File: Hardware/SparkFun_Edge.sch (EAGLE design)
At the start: 64 parts, among them J5 CORTEX_DEBUG, J7 CAMERA-HIMAX, U2 LIS2DH12, U3 1.8V, U5 ARTEMIS_MODULESMD, Y2 32.768kHz

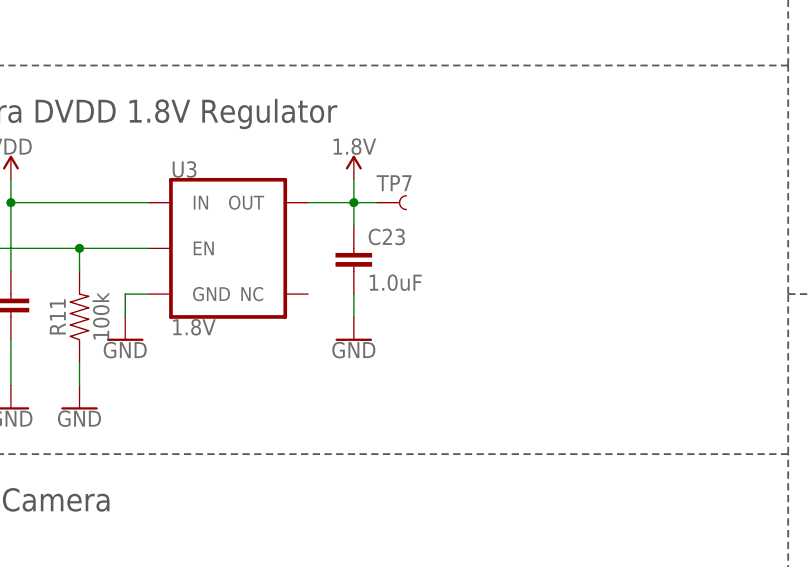
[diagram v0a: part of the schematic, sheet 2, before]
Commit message: Rename files. Remove dependancy on Ambiq lbr. Remove ambiq.lbr.
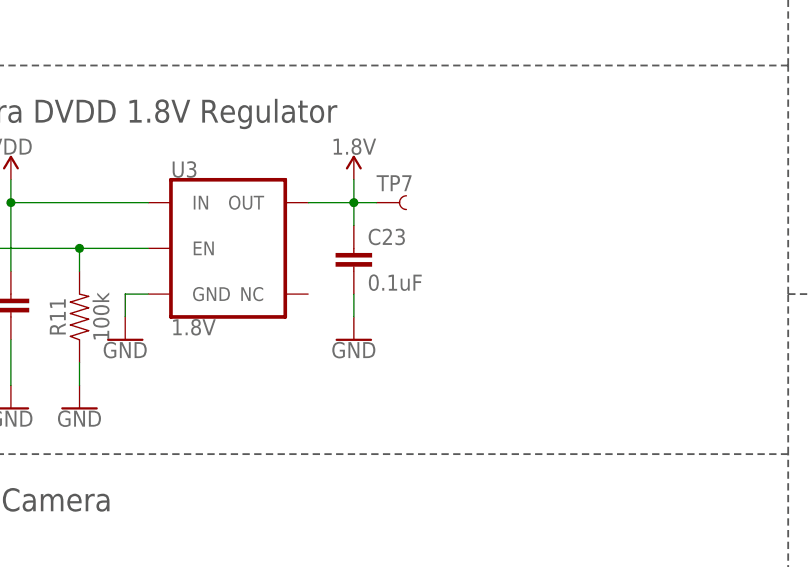
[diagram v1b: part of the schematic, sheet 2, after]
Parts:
- C1, C18, C20: device ambiq:0.1UF-0402-TIGHT-16V-10% -> SparkFun-Capacitors:0.1UF-0402T-16V-10%
- C10, C9: device ambiq:15PF-0402-TIGHT-50V-5% -> SparkFun-Capacitors:15PF-0402T-50V-5%
- C22: device ambiq:1.0UF-0402-TIGHT-16V-10% -> SparkFun-Capacitors:1.0UF-0402T-16V-10%
- C23: value 1.0uF -> 0.1uF; device ambiq:1.0UF-0402-TIGHT-16V-10% -> SparkFun-Capacitors:0.1UF-0402T-16V-10%
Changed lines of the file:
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@@
 <?xml version="1.0" encoding="utf-8"?>
 <!DOCTYPE eagle SYSTEM "eagle.dtd">
-<eagle version="9.5.1">
+<eagle version="9.4.2">
 <drawing>
 <settings>
@@
 <part name="J2" library="SparkFun-Connectors" deviceset="6_PIN_SERIAL_TARGET" device="SMD"/>
 <part name="Y2" library="SparkFun-Clocks" deviceset="CRYSTAL-32.768KHZ" device="SMD-3.2X1.5" value="32.768kHz"/>
-<part name="C9" library="ambiq" deviceset="15PF" device="-0402-TIGHT-50V-5%" value="15pF"/>
-<part name="C10" library="ambiq" deviceset="15PF" device="-0402-TIGHT-50V-5%" value="15pF"/>
+<part name="C9" library="SparkFun-Capacitors" deviceset="15PF" device="-0402T-50V-5%" value="15pF"/>
+<part name="C10" library="SparkFun-Capacitors" deviceset="15PF" device="-0402T-50V-5%" value="15pF"/>
 <part name="GND19" library="SparkFun-PowerSymbols" deviceset="GND" device=""/>
 <part name="GND24" library="SparkFun-PowerSymbols" deviceset="GND" device=""/>
@@
 <part name="U2" library="SparkFun-Sensors" deviceset="LIS2DH12" device=""/>
 <part name="C21" library="SparkFun-Capacitors" deviceset="10UF" device="-0603-6.3V-20%" value="10uF"/>
-<part name="C20" library="ambiq" deviceset="0.1UF" device="-0402-TIGHT-16V-10%" value="0.1uF"/>
+<part name="C20" library="SparkFun-Capacitors" deviceset="0.1UF" device="-0402T-16V-10%" value="0.1uF"/>
 <part name="GND31" library="SparkFun-PowerSymbols" deviceset="GND" device=""/>
 <part name="GND29" library="SparkFun-PowerSymbols" deviceset="GND" device=""/>
@@
 <part name="GND34" library="SparkFun-PowerSymbols" deviceset="GND" device=""/>
 <part name="SUPPLY28" library="SparkFun-PowerSymbols" deviceset="1.8V" device=""/>
-<part name="C22" library="ambiq" deviceset="1.0UF" device="-0402-TIGHT-16V-10%" value="1.0uF"/>
-<part name="C23" library="ambiq" deviceset="1.0UF" device="-0402-TIGHT-16V-10%" value="1.0uF"/>
+<part name="C22" library="SparkFun-Capacitors" deviceset="1.0UF" device="-0402T-16V-10%" value="1.0uF"/>
+<part name="C23" library="SparkFun-Capacitors" deviceset="0.1UF" device="-0402T-16V-10%" value="0.1uF"/>
 <part name="GND35" library="SparkFun-PowerSymbols" deviceset="GND" device=""/>
 <part name="GND30" library="SparkFun-PowerSymbols" deviceset="GND" device=""/>
@@
 <part name="GND45" library="SparkFun-PowerSymbols" deviceset="GND" device=""/>
 <part name="GND17" library="SparkFun-PowerSymbols" deviceset="GND" device=""/>
-<part name="C18" library="ambiq" deviceset="0.1UF" device="-0402-TIGHT-16V-10%" value="0.1uF"/>
+<part name="C18" library="SparkFun-Capacitors" deviceset="0.1UF" device="-0402T-16V-10%" value="0.1uF"/>
 <part name="GND21" library="SparkFun-PowerSymbols" deviceset="GND" device=""/>
 <part name="GND36" library="SparkFun-PowerSymbols" deviceset="GND" device=""/>
@@
 <part name="GND7" library="SparkFun-PowerSymbols" deviceset="GND" device=""/>
 <part name="E2" library="SparkFun-Sensors" deviceset="SPH0641LM4H-1_MICROPHONE" device="" value="SPH0641LM4H-1"/>
-<part name="C1" library="ambiq" deviceset="0.1UF" device="-0402-TIGHT-16V-10%" value="0.1uF"/>
+<part name="C1" library="SparkFun-Capacitors" deviceset="0.1UF" device="-0402T-16V-10%" value="0.1uF"/>
 <part name="GND2" library="SparkFun-PowerSymbols" deviceset="GND" device=""/>
 <part name="GND8" library="SparkFun-PowerSymbols" deviceset="GND" device=""/>

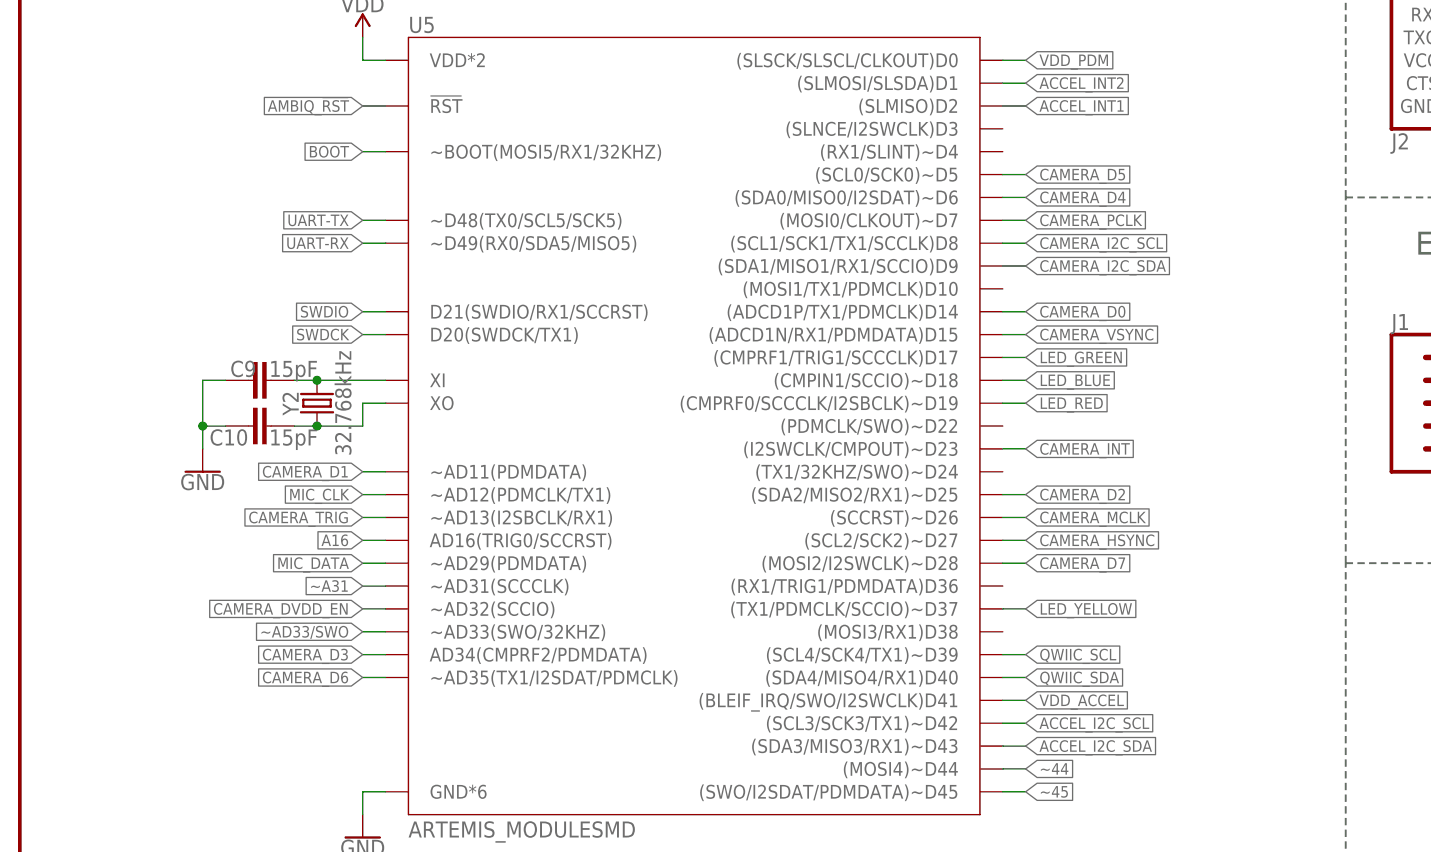
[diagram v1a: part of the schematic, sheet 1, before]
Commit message: add gpio numbers to camera nets for ease of use
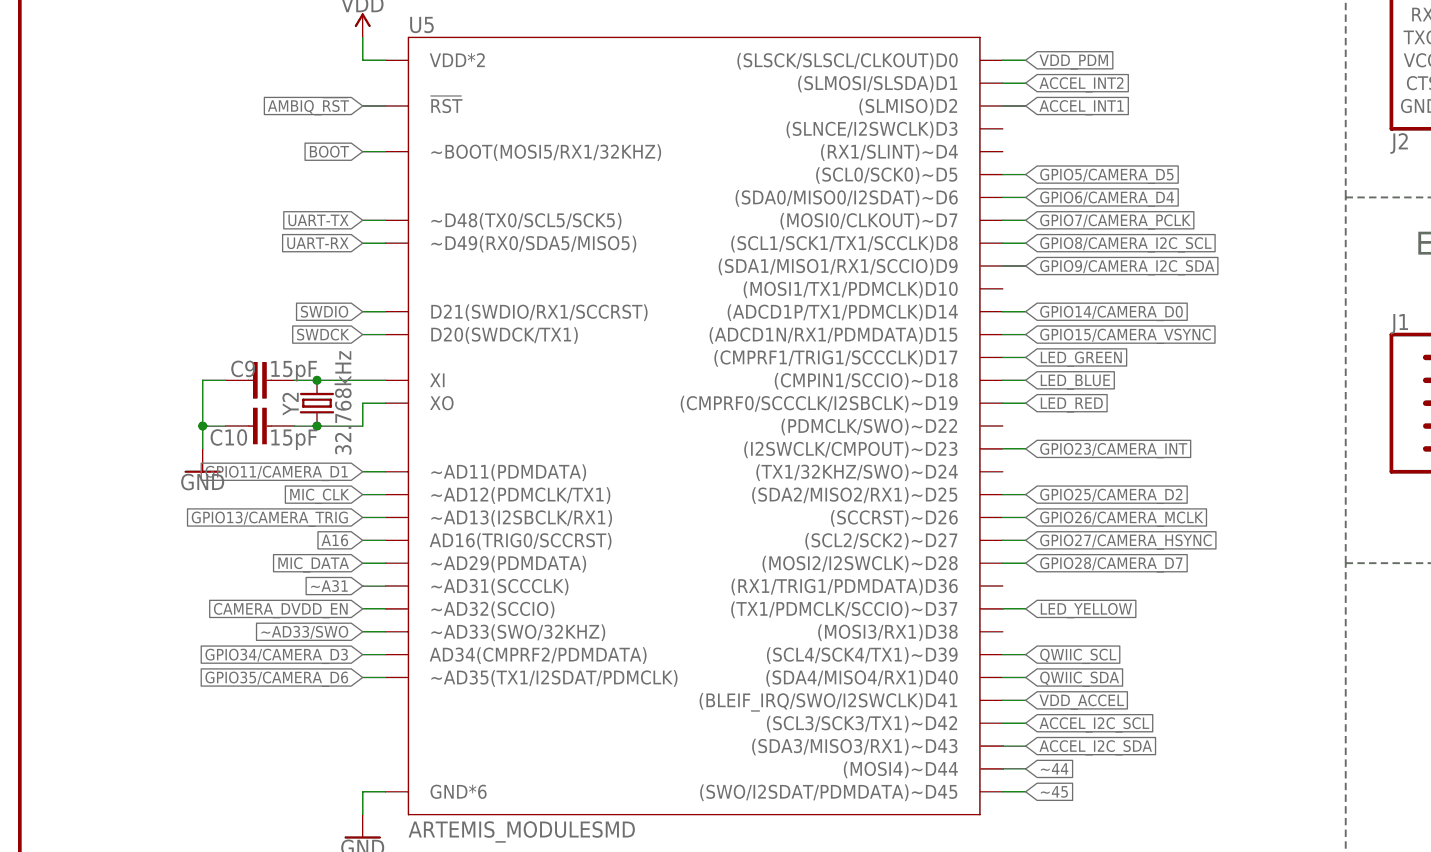
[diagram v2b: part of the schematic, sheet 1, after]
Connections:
- net CAMERA_D0 renamed GPIO14/CAMERA_D0
- net CAMERA_D1 renamed GPIO11/CAMERA_D1
- net CAMERA_D2 renamed GPIO25/CAMERA_D2
- net CAMERA_D3 renamed GPIO34/CAMERA_D3
- net CAMERA_D4 renamed GPIO6/CAMERA_D4
- net CAMERA_D5 renamed GPIO5/CAMERA_D5
- net CAMERA_D6 renamed GPIO35/CAMERA_D6
- net CAMERA_D7 renamed GPIO28/CAMERA_D7
- net CAMERA_HSYNC renamed GPIO27/CAMERA_HSYNC
- net CAMERA_I2C_SCL renamed GPIO8/CAMERA_I2C_SCL
- net CAMERA_I2C_SDA renamed GPIO9/CAMERA_I2C_SDA
- net CAMERA_INT renamed GPIO23/CAMERA_INT
- net CAMERA_MCLK renamed GPIO26/CAMERA_MCLK
- net CAMERA_PCLK renamed GPIO7/CAMERA_PCLK
- net CAMERA_TRIG renamed GPIO13/CAMERA_TRIG
- net CAMERA_VSYNC renamed GPIO15/CAMERA_VSYNC
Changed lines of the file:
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@@
 <?xml version="1.0" encoding="utf-8"?>
 <!DOCTYPE eagle SYSTEM "eagle.dtd">
-<eagle version="9.4.2">
+<eagle version="9.5.0">
 <drawing>
 <settings>
@@
 </segment>
 </net>
-<net name="CAMERA_VSYNC" class="0">
+<net name="GPIO15/CAMERA_VSYNC" class="0">
 <segment>
 <wire x1="109.22" y1="93.98" x2="111.76" y2="93.98" width="0.1524" layer="91"/>
@@
 </segment>
 </net>
-<net name="CAMERA_INT" class="0">
+<net name="GPIO23/CAMERA_INT" class="0">
 <segment>
 <wire x1="109.22" y1="81.28" x2="111.76" y2="81.28" width="0.1524" layer="91"/>
@@
 </segment>
 </net>
-<net name="CAMERA_I2C_SDA" class="0">
-<segment>
-<wire x1="109.22" y1="101.6" x2="111.76" y2="101.6" width="0.1524" layer="91"/>
-<label x="111.76" y="101.6" size="1.27" layer="95" xref="yes"/>
-<pinref part="U5" gate="U1" pin="(SDA1/MISO1/RX1/SCCIO)D9"/>
-</segment>
-</net>
-<net name="CAMERA_I2C_SCL" class="0">
+<net name="GPIO8/CAMERA_I2C_SCL" class="0">
 <segment>
 <wire x1="109.22" y1="104.14" x2="111.76" y2="104.14" width="0.1524" layer="91"/>
@@
 </segment>
 </net>
-<net name="CAMERA_TRIG" class="0">
+<net name="GPIO13/CAMERA_TRIG" class="0">
 <segment>
 <wire x1="40.64" y1="73.66" x2="38.1" y2="73.66" width="0.1524" layer="91"/>
@@
 </segment>
 </net>
-<net name="CAMERA_HSYNC" class="0">
+<net name="GPIO27/CAMERA_HSYNC" class="0">
 <segment>
 <wire x1="109.22" y1="71.12" x2="111.76" y2="71.12" width="0.1524" layer="91"/>
@@
 </segment>
 </net>
-<net name="CAMERA_D7" class="0">
+<net name="GPIO28/CAMERA_D7" class="0">
 <segment>
 <wire x1="109.22" y1="68.58" x2="111.76" y2="68.58" width="0.1524" layer="91"/>
@@
 </segment>
 </net>
-<net name="CAMERA_D6" class="0">
+<net name="GPIO35/CAMERA_D6" class="0">
 <segment>
 <wire x1="40.64" y1="55.88" x2="38.1" y2="55.88" width="0.1524" layer="91"/>
@@
 </segment>
 </net>
-<net name="CAMERA_D5" class="0">
+<net name="GPIO5/CAMERA_D5" class="0">
 <segment>
 <wire x1="109.22" y1="111.76" x2="111.76" y2="111.76" width="0.1524" layer="91"/>
@@
 </segment>
 </net>
-<net name="CAMERA_PCLK" class="0">
+<net name="GPIO7/CAMERA_PCLK" class="0">
 <segment>
 <wire x1="109.22" y1="106.68" x2="111.76" y2="106.68" width="0.1524" layer="91"/>
@@
 </segment>
 </net>
-<net name="CAMERA_D4" class="0">
+<net name="GPIO6/CAMERA_D4" class="0">
 <segment>
 <wire x1="109.22" y1="109.22" x2="111.76" y2="109.22" width="0.1524" layer="91"/>
@@
 </segment>
 </net>
-<net name="CAMERA_D0" class="0">
+<net name="GPIO14/CAMERA_D0" class="0">
 <segment>
 <wire x1="109.22" y1="96.52" x2="111.76" y2="96.52" width="0.1524" layer="91"/>
@@
 </segment>
 </net>
-<net name="CAMERA_D3" class="0">
+<net name="GPIO34/CAMERA_D3" class="0">
 <segment>
 <wire x1="40.64" y1="58.42" x2="38.1" y2="58.42" width="0.1524" layer="91"/>
@@
 </segment>
 </net>
-<net name="CAMERA_D1" class="0">
+<net name="GPIO11/CAMERA_D1" class="0">
 <segment>
 <wire x1="40.64" y1="78.74" x2="38.1" y2="78.74" width="0.1524" layer="91"/>
@@
 </segment>
 </net>
-<net name="CAMERA_D2" class="0">
+<net name="GPIO25/CAMERA_D2" class="0">
 <segment>
 <wire x1="109.22" y1="76.2" x2="111.76" y2="76.2" width="0.1524" layer="91"/>
@@
 </segment>
 </net>
-<net name="CAMERA_MCLK" class="0">
+<net name="GPIO26/CAMERA_MCLK" class="0">
 <segment>
 <wire x1="109.22" y1="73.66" x2="111.76" y2="73.66" width="0.1524" layer="91"/>
@@
 <wire x1="109.22" y1="53.34" x2="111.76" y2="53.34" width="0.1524" layer="91"/>
 <label x="111.76" y="53.34" size="1.27" layer="95" xref="yes"/>
+</segment>
+</net>
+<net name="GPIO9/CAMERA_I2C_SDA" class="0">
+<segment>
+<wire x1="109.22" y1="101.6" x2="111.76" y2="101.6" width="0.1524" layer="91"/>
+<label x="111.76" y="101.6" size="1.27" layer="95" xref="yes"/>
+<pinref part="U5" gate="U1" pin="(SDA1/MISO1/RX1/SCCIO)D9"/>
 </segment>
 </net>
@@
 </segment>
 </net>
-<net name="CAMERA_I2C_SCL" class="0">
+<net name="GPIO8/CAMERA_I2C_SCL" class="0">
 <segment>
 <wire x1="86.36" y1="58.42" x2="88.9" y2="58.42" width="0.1524" layer="91"/>
@@
 </segment>
 </net>
-<net name="CAMERA_I2C_SDA" class="0">
+<net name="GPIO9/CAMERA_I2C_SDA" class="0">
 <segment>
 <wire x1="86.36" y1="55.88" x2="88.9" y2="55.88" width="0.1524" layer="91"/>
@@
 </segment>
 </net>
-<net name="CAMERA_D1" class="0">
+<net name="GPIO11/CAMERA_D1" class="0">
 <segment>
 <wire x1="86.36" y1="33.02" x2="88.9" y2="33.02" width="0.1524" layer="91"/>
@@
 </segment>
 </net>
-<net name="CAMERA_D3" class="0">
+<net name="GPIO34/CAMERA_D3" class="0">
 <segment>
 <wire x1="86.36" y1="27.94" x2="88.9" y2="27.94" width="0.1524" layer="91"/>
@@
 </segment>
 </net>
-<net name="CAMERA_D4" class="0">
+<net name="GPIO6/CAMERA_D4" class="0">
 <segment>
 <wire x1="86.36" y1="25.4" x2="88.9" y2="25.4" width="0.1524" layer="91"/>
@@
 </segment>
 </net>
-<net name="CAMERA_D5" class="0">
+<net name="GPIO5/CAMERA_D5" class="0">
 <segment>
 <wire x1="86.36" y1="22.86" x2="88.9" y2="22.86" width="0.1524" layer="91"/>
@@
 </segment>
 </net>
-<net name="CAMERA_D6" class="0">
+<net name="GPIO35/CAMERA_D6" class="0">
 <segment>
 <wire x1="86.36" y1="20.32" x2="88.9" y2="20.32" width="0.1524" layer="91"/>
@@
 </segment>
 </net>
-<net name="CAMERA_D7" class="0">
+<net name="GPIO28/CAMERA_D7" class="0">
 <segment>
 <wire x1="86.36" y1="17.78" x2="88.9" y2="17.78" width="0.1524" layer="91"/>
@@
 </segment>
 </net>
-<net name="CAMERA_VSYNC" class="0">
+<net name="GPIO15/CAMERA_VSYNC" class="0">
 <segment>
 <wire x1="86.36" y1="50.8" x2="88.9" y2="50.8" width="0.1524" layer="91"/>
@@
 </segment>
 </net>
-<net name="CAMERA_HSYNC" class="0">
+<net name="GPIO27/CAMERA_HSYNC" class="0">
 <segment>
 <wire x1="86.36" y1="48.26" x2="88.9" y2="48.26" width="0.1524" layer="91"/>
@@
 </segment>
 </net>
-<net name="CAMERA_PCLK" class="0">
+<net name="GPIO7/CAMERA_PCLK" class="0">
 <segment>
 <wire x1="86.36" y1="40.64" x2="88.9" y2="40.64" width="0.1524" layer="91"/>
@@
 </segment>
 </net>
-<net name="CAMERA_D0" class="0">
+<net name="GPIO14/CAMERA_D0" class="0">
 <segment>
 <wire x1="86.36" y1="35.56" x2="88.9" y2="35.56" width="0.1524" layer="91"/>
@@
 </segment>
 </net>
-<net name="CAMERA_D2" class="0">
+<net name="GPIO25/CAMERA_D2" class="0">
 <segment>
 <wire x1="86.36" y1="30.48" x2="88.9" y2="30.48" width="0.1524" layer="91"/>
@@
 </segment>
 </net>
-<net name="CAMERA_TRIG" class="0">
+<net name="GPIO13/CAMERA_TRIG" class="0">
 <segment>
 <wire x1="60.96" y1="45.72" x2="58.42" y2="45.72" width="0.1524" layer="91"/>
@@
 </segment>
 </net>
-<net name="CAMERA_INT" class="0">
+<net name="GPIO23/CAMERA_INT" class="0">
 <segment>
 <wire x1="60.96" y1="43.18" x2="58.42" y2="43.18" width="0.1524" layer="91"/>
@@
 </segment>
 </net>
-<net name="CAMERA_MCLK" class="0">
+<net name="GPIO26/CAMERA_MCLK" class="0">
 <segment>
 <wire x1="86.36" y1="43.18" x2="88.9" y2="43.18" width="0.1524" layer="91"/>
